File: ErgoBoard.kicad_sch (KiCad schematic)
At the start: 67 parts, among them SW1 SW_Push, SW10 SW_Push, SW11 SW_Push, SW12 SW_Push, SW13 SW_Push, SW14 SW_Push, SW15 SW_Push, SW16 SW_Push, SW17 SW_Push, SW18 SW_Push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

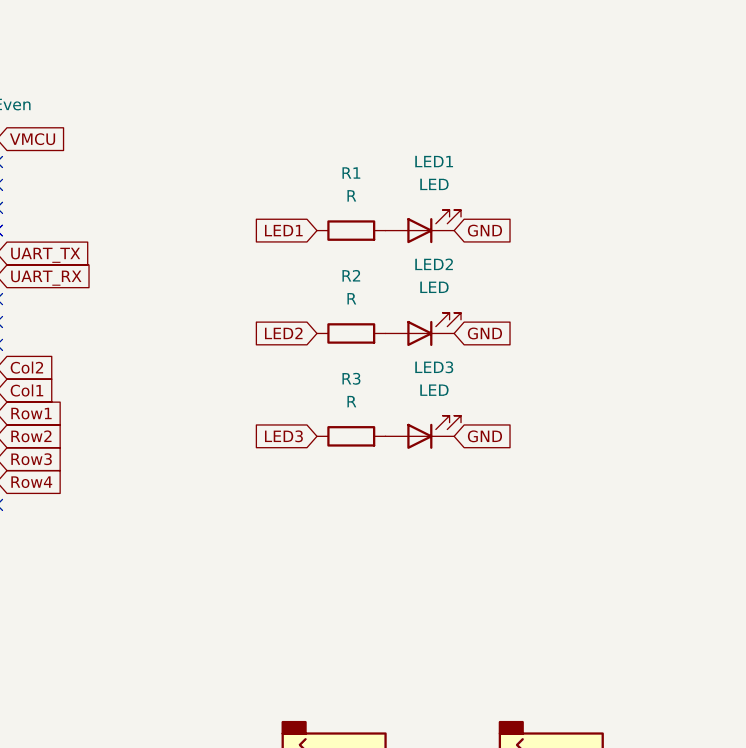
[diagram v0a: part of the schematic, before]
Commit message: Add UART debug test points
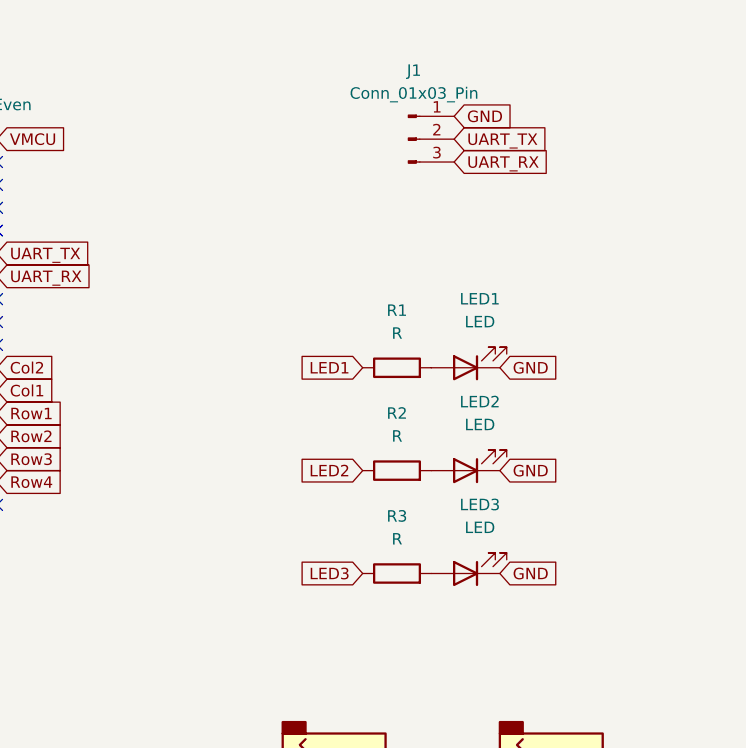
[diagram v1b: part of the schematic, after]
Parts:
- added J1: Conn_01x03_Pin, Connector_PinHeader_2.54mm:PinHeader_1x03_P2.54mm_Vertical, symbol Connector:Conn_01x03_Pin
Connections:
- net GND: now also J1.1 (Pin_1)
- net UART_RX: now also J1.3 (Pin_3)
- net UART_TX: now also J1.2 (Pin_2)
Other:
- moved on the sheet: LED1, LED2, LED3, R1, R2, R3

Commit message: Update schematic pdf
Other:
- title: (none) -> ErgoBergo
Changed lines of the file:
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@@
 (kicad_sch (version 20230121) (generator eeschema)
   (paper "A4")
+  (title_block
+    (title "ErgoBergo")
+    (date "2025-01-12")
+    (rev "1.1")
+  )
   (junction (at 107.95 148.59) (diameter 0) (color 0 0 0 0)
   )
